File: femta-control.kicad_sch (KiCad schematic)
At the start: 12 parts, among them U4 LM358-N-Q1

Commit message: some stuff
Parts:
- added J2: CUBESAT INTERFACE, symbol Connector_Generic:Conn_02x05_Odd_Even
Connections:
- net +3.3V: now also J2.4 (Pin_4)
- net +5V: now also J2.2 (Pin_2)
- net +5VP: now also J2.3 (Pin_3)
- net +BATT: now also J2.1 (Pin_1)
- net GND: now also J2.5 (Pin_5), J2.7 (Pin_7), J2.9 (Pin_9)
- new net I2C_SCL: J2.10 (Pin_10)
- new net I2C_SDA: J2.8 (Pin_8)
- new net OCP_RST: J2.6 (Pin_6)
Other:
- sheet Thermal Circuit 1 renamed FEMTA Thermal Circuit 1
- added sheet 5V Protection (OCP.kicad_sch)
- added sheet FEMTA Thermal Circuit 10 (thermal-subcircuit.kicad_sch)
- added sheet FEMTA Thermal Circuit 11 (thermal-subcircuit.kicad_sch)
- added sheet FEMTA Thermal Circuit 12 (thermal-subcircuit.kicad_sch)
- added sheet FEMTA Thermal Circuit 2 (thermal-subcircuit.kicad_sch)
- added sheet FEMTA Thermal Circuit 3 (thermal-subcircuit.kicad_sch)
- added sheet FEMTA Thermal Circuit 4 (thermal-subcircuit.kicad_sch)
- added sheet FEMTA Thermal Circuit 5 (thermal-subcircuit.kicad_sch)
- added sheet FEMTA Thermal Circuit 6 (thermal-subcircuit.kicad_sch)
- added sheet FEMTA Thermal Circuit 7 (thermal-subcircuit.kicad_sch)
- added sheet FEMTA Thermal Circuit 8 (thermal-subcircuit.kicad_sch)
- added sheet FEMTA Thermal Circuit 9 (thermal-subcircuit.kicad_sch)
- added sheet Tank Thermal Circuit 1 (thermal-subcircuit.kicad_sch)
- added sheet Tank Thermal Circuit 2 (thermal-subcircuit.kicad_sch)
- added sheet Tank Thermal Circuit 3 (thermal-subcircuit.kicad_sch)
- added sheet Tank Thermal Circuit 4 (thermal-subcircuit.kicad_sch)
- moved on the sheet: C6, RV1, RV2, U4A, U4B, U4C

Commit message: ocp channels
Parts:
- added R122, R125, R127, R134, R135, R136, R139: 10K, symbol Device:R
- added R124, R126: 0, symbol Device:R
- added R133: 30K, symbol Device:R
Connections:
- net +3.3V: now also R139.1; no longer J2.4 (Pin_4)
- net +5V: no longer J2.2 (Pin_2)
- net +5VP: no longer J2.3 (Pin_3)
- net +BATT: no longer J2.1 (Pin_1)
- net GND: now also R125.2, R127.2, R134.2, R136.2
- net OCP_RST: now also R122.2
- new net 3.3V LCL/COMP_IN: R126.2, R127.1
- new net 3.3V LCL/I_OUT: R126.1
- new net 3.3V_UNPROT: J2.4 (Pin_4), R122.1
- new net 5V LCL/COMP_IN: R124.2, R125.1
- new net 5V LCL/I_OUT: R124.1
- new net 5V LCL1/COMP_IN: R135.2, R136.1
- new net 5V LCL1/I_OUT: R135.1
- new net 5V_HEATER_UNPROT: J2.3 (Pin_3)
- new net 5V_UNPROT: J2.2 (Pin_2)
- new net BATT LCL/COMP_IN: R133.2, R134.1
- new net BATT LCL/I_OUT: R133.1
- new net BATT_UNPROT: J2.1 (Pin_1)
- new net HEATER_RST: R139.2
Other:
- removed sheet 5V Protection
- added sheet 3.3V LCL (LCL_LV.kicad_sch)
- added sheet 5V LCL (LCL_LV.kicad_sch)
- added sheet 5V LCL1 (LCL_LV.kicad_sch)
- added sheet BATT LCL (LCL_HV.kicad_sch)

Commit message: i2c
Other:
- sheet Microcontroller ports: added I2C_MASTER_SCL, I2C_MASTER_SDA, I2C_SLAVE_SCL, I2C_SLAVE_SDA; removed none
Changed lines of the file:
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@@
 	(wire
 		(pts
+			(xy 104.14 114.3) (xy 95.25 114.3)
+		)
+		(stroke
+			(width 0)
+			(type default)
+		)
+	)
+	(wire
+		(pts
 			(xy 44.45 111.76) (xy 44.45 114.3)
 		)
@@
 	(wire
 		(pts
+			(xy 104.14 116.84) (xy 95.25 116.84)
+		)
+		(stroke
+			(width 0)
+			(type default)
+		)
+	)
+	(wire
+		(pts
 			(xy 138.43 73.66) (xy 138.43 68.58)
 		)
@@
 		)
 	)
+	(label "I2C_SCL"
+		(at 95.25 114.3 0)
+		(fields_autoplaced yes)
+		(effects
+			(font
+				(size 1.27 1.27)
+			)
+			(justify left bottom)
+		)
+	)
 	(label "I2C_SDA"
 		(at 69.85 114.3 180)
@@
 		)
 	)
+	(label "I2C_SDA"
+		(at 95.25 116.84 0)
+		(fields_autoplaced yes)
+		(effects
+			(font
+				(size 1.27 1.27)
+			)
+			(justify left bottom)
+		)
+	)
 	(label "OCP_RST"
 		(at 69.85 111.76 180)
@@
 	)
 	(sheet
-		(at 53.34 53.34)
+		(at 104.14 109.22)
 		(size 35.56 26.67)
 		(fields_autoplaced yes)
@@
 		)
 		(property "Sheetname" "Microcontroller"
-			(at 53.34 52.6284 0)
+			(at 104.14 108.5084 0)
 			(effects
 				(font
@@
 		)
 		(property "Sheetfile" "microcontroller.kicad_sch"
-			(at 53.34 80.5946 0)
+			(at 104.14 136.4746 0)
 			(effects
 				(font
@@
 			)
 		)
+		(pin "I2C_MASTER_SDA" input
+			(at 139.7 116.84 0)
+			(effects
+				(font
+					(size 1.27 1.27)
+				)
+				(justify right)
+			)
+		)
+		(pin "I2C_MASTER_SCL" input
+			(at 139.7 114.3 0)
+			(effects
+				(font
+					(size 1.27 1.27)
+				)
+				(justify right)
+			)
+		)
+		(pin "I2C_SLAVE_SCL" input
+			(at 104.14 114.3 180)
+			(effects
+				(font
+					(size 1.27 1.27)
+				)
+				(justify left)
+			)
+		)
+		(pin "I2C_SLAVE_SDA" input
+			(at 104.14 116.84 180)
+			(effects
+				(font
+					(size 1.27 1.27)
+				)
+				(justify left)
+			)
+		)

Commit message: work
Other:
- added sheet Thruster Control (thrust-control-master.kicad_sch)
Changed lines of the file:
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@@
+	)
+	(sheet
+		(at 238.76 199.39)
+		(size 39.37 24.13)
+		(fields_autoplaced yes)
+		(stroke
+			(width 0.1524)
+			(type solid)
+		)
+		(fill
+			(color 0 0 0 0.0000)
+		)
+		(property "Sheetname" "Thruster Control"
+			(at 238.76 198.6784 0)
+			(effects
+				(font
+					(size 1.27 1.27)
+				)
+				(justify left bottom)
+			)
+		)
+		(property "Sheetfile" "thrust-control-master.kicad_sch"
+			(at 238.76 224.1046 0)
+			(effects
+				(font
+					(size 1.27 1.27)
+				)
+				(justify left top)
+			)
+		)
+		(instances
+			(project "femta-control"
+				(path "/838bf11c-36b7-41d7-9462-fe98a188d617"
+					(page "23")
+				)
+			)
+		)
 	)
 	(sheet

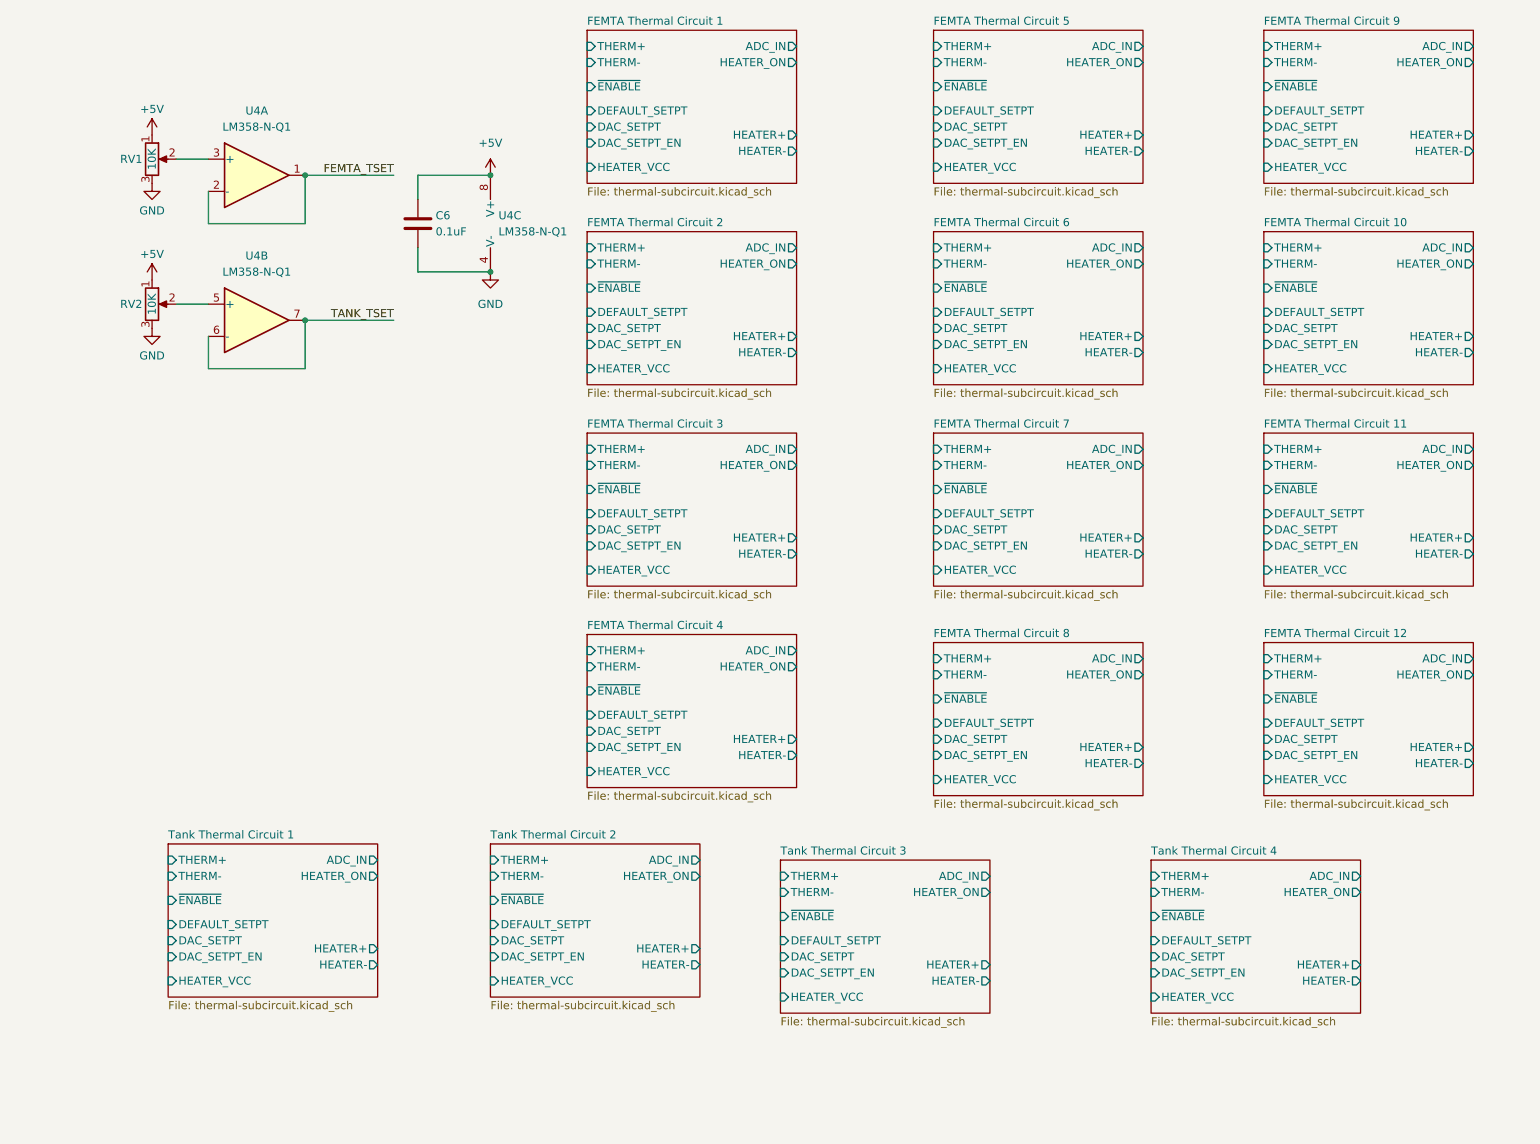
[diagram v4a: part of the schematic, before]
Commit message: dpt sheet and move thermals into subsheet
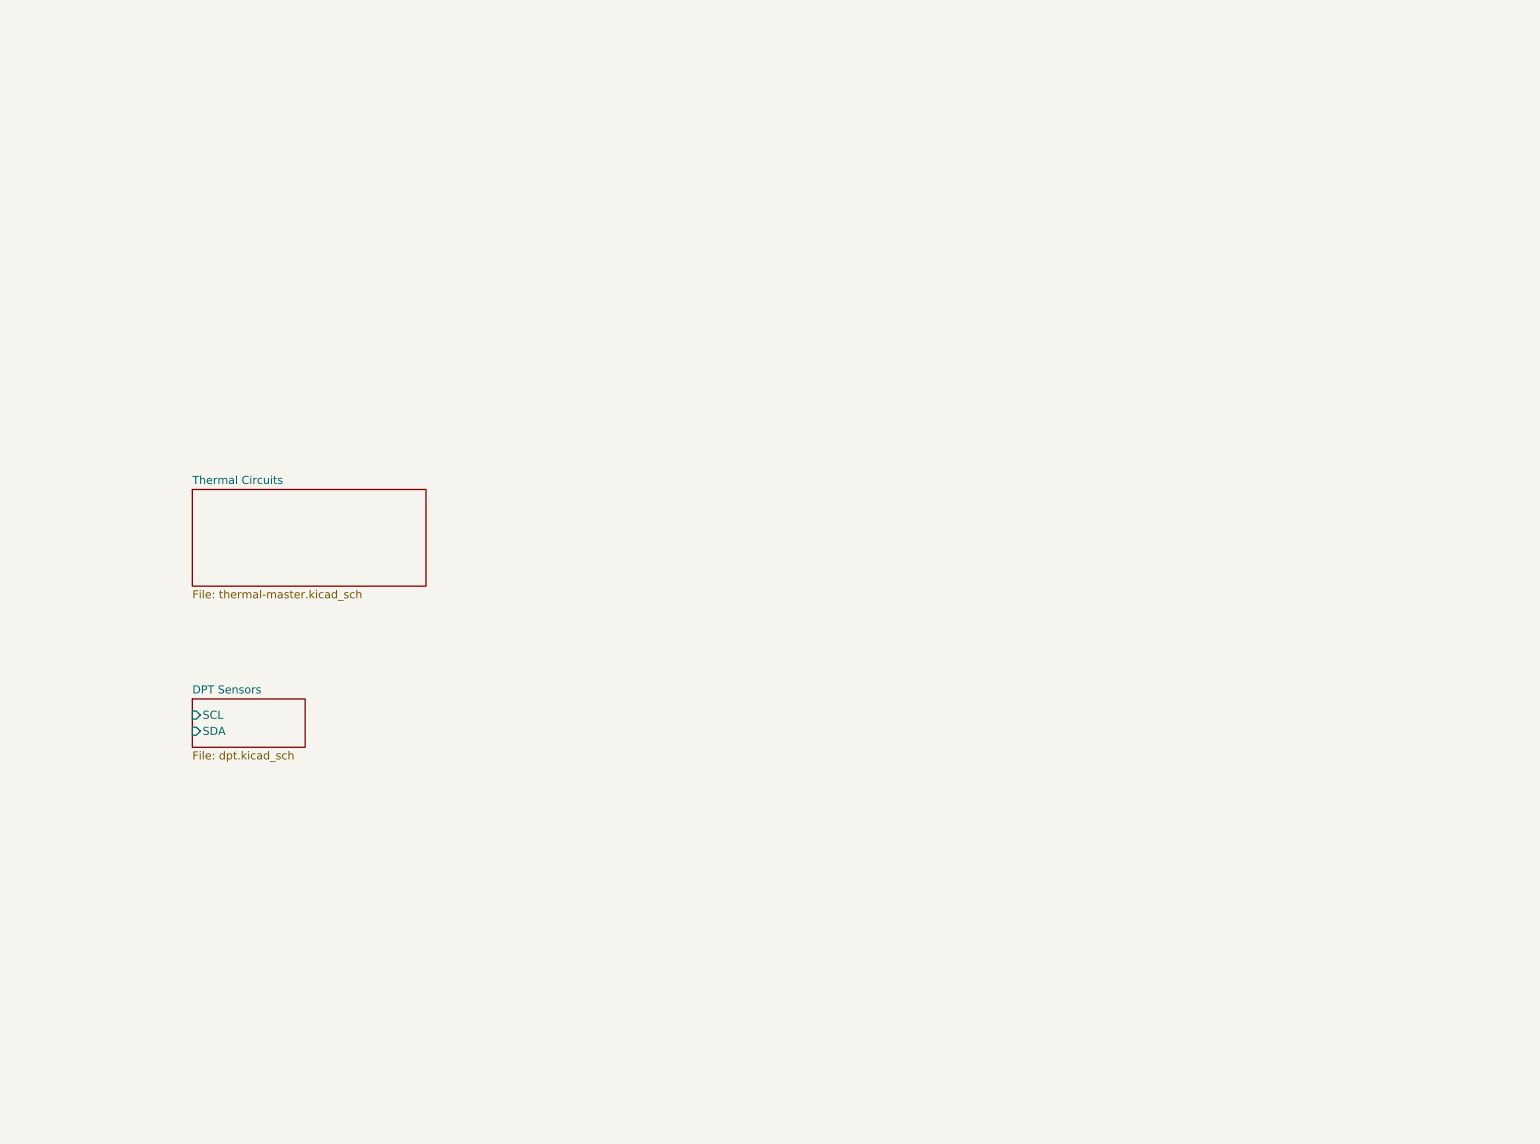
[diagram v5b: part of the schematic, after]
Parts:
- removed C6: 0.1uF, symbol Device:C
- removed RV1, RV2: 10K, symbol Device:R_Potentiometer
- removed U4: LM358-N-Q1, symbol Amplifier_Operational:LM358
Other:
- removed sheet FEMTA Thermal Circuit 1
- removed sheet FEMTA Thermal Circuit 10
- removed sheet FEMTA Thermal Circuit 11
- removed sheet FEMTA Thermal Circuit 12
- removed sheet FEMTA Thermal Circuit 2
- removed sheet FEMTA Thermal Circuit 3
- removed sheet FEMTA Thermal Circuit 4
- removed sheet FEMTA Thermal Circuit 5
- removed sheet FEMTA Thermal Circuit 6
- removed sheet FEMTA Thermal Circuit 7
- removed sheet FEMTA Thermal Circuit 8
- removed sheet FEMTA Thermal Circuit 9
- removed sheet Tank Thermal Circuit 1
- removed sheet Tank Thermal Circuit 2
- removed sheet Tank Thermal Circuit 3
- removed sheet Tank Thermal Circuit 4
- added sheet DPT Sensors (dpt.kicad_sch)
- added sheet Thermal Circuits (thermal-master.kicad_sch)

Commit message: syms
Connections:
- net HEATER 5V LCL/I_OUT renamed I_FEMTA_HEATER
- net HEATER_RST renamed HEATER_OCP_RST
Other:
- sheet 5V LCL1 renamed HEATER 5V LCL
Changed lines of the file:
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@@
 	(paper "USLedger")
 	(junction
+		(at 168.91 160.02)
+		(diameter 0)
+		(color 0 0 0 0)
+	)
+	(junction
 		(at 106.68 204.47)
 		(diameter 0)
@@
 	(wire
 		(pts
-			(xy 119.38 167.64) (xy 134.62 167.64)
+			(xy 116.84 167.64) (xy 134.62 167.64)
 		)
 		(stroke
@@
 	(wire
 		(pts
+			(xy 168.91 160.02) (xy 185.42 160.02)
+		)
+		(stroke
+			(width 0)
+			(type default)
+		)
+	)
+	(wire
+		(pts
 			(xy 100.33 204.47) (xy 106.68 204.47)
 		)
@@
 		)
 	)
-	(label "HEATER_RST"
-		(at 119.38 167.64 0)
+	(label "HEATER_OCP_RST"
+		(at 116.84 167.64 0)
 		(fields_autoplaced yes)
 		(effects
@@
 		)
 	)
+	(label "I_FEMTA_HEATER"
+		(at 185.42 160.02 180)
+		(fields_autoplaced yes)
+		(effects
+			(font
+				(size 1.27 1.27)
+			)
+			(justify right bottom)
+		)
+	)
 	(label "OCP_RST"
 		(at 62.23 182.88 0)
@@
 	)
 	(symbol
+		(lib_id "power:+5VP")
+		(at 168.91 154.94 0)
+		(unit 1)
+		(exclude_from_sim no)
+		(in_bom yes)
+		(on_board yes)
+		(dnp no)
+		(fields_autoplaced yes)
+		(property "Reference" "#PWR015"
+			(at 168.91 158.75 0)
+			(effects
+				(font
+					(size 1.27 1.27)
+				)
+				(hide yes)
+			)
+		)
+		(property "Value" "+5VP"
+			(at 168.91 149.86 0)
+			(effects
+				(font
+					(size 1.27 1.27)
+				)
+			)
+		)
+		(property "Footprint" ""
+			(at 168.91 154.94 0)
+			(effects
+				(font
+					(size 1.27 1.27)
+				)
+				(hide yes)
+			)
+		)
+		(property "Datasheet" ""
+			(at 168.91 154.94 0)
+			(effects
+				(font
+					(size 1.27 1.27)
+				)
+				(hide yes)
+			)
+		)
+		(property "Description" "Power symbol creates a global label with name \"+5VP\""
+			(at 168.91 154.94 0)
+			(effects
+				(font
+					(size 1.27 1.27)
+				)
+				(hide yes)
+			)
+		)
+		(pin "1"
+		)
+		(instances
+			(project "femta-control"
+				(path "/838bf11c-36b7-41d7-9462-fe98a188d617"
+					(reference "#PWR015")
+					(unit 1)
+				)
+			)
+		)
+	)
+	(symbol
 		(lib_id "Device:R")
 		(at 128.27 57.15 0)
@@
 	)
 	(symbol
-		(lib_id "power:+5VP")
-		(at 168.91 154.94 0)
-		(unit 1)
-		(exclude_from_sim no)
-		(in_bom yes)
-		(on_board yes)
-		(dnp no)
-		(fields_autoplaced yes)
-		(property "Reference" "#PWR0198"
-			(at 168.91 158.75 0)
-			(effects
-				(font
-					(size 1.27 1.27)
-				)
-				(hide yes)
-			)
-		)
-		(property "Value" "+5VP"
-			(at 168.91 149.86 0)
-			(effects
-				(font
-					(size 1.27 1.27)
-				)
-			)
-		)
-		(property "Footprint" ""
-			(at 168.91 154.94 0)
-			(effects
-				(font
-					(size 1.27 1.27)
-				)
-				(hide yes)
-			)
-		)
-		(property "Datasheet" ""
-			(at 168.91 154.94 0)
-			(effects
-				(font
-					(size 1.27 1.27)
-				)
-				(hide yes)
-			)
-		)
-		(property "Description" "Power symbol creates a global label with name \"+5VP\""
-			(at 168.91 154.94 0)
-			(effects
-				(font
-					(size 1.27 1.27)
-				)
-				(hide yes)
-			)
-		)
-		(pin "1"
-		)
-		(instances
-			(project "femta-control"
-				(path "/838bf11c-36b7-41d7-9462-fe98a188d617"
-					(reference "#PWR0198")
-					(unit 1)
-				)
-			)
-		)
-	)
-	(symbol
 		(lib_id "Device:R")
 		(at 106.68 163.83 0)
@@
 			(color 0 0 0 0.0000)
 		)
-		(property "Sheetname" "5V LCL1"
+		(property "Sheetname" "HEATER 5V LCL"
 			(at 140.97 151.6884 0)
 			(effects
